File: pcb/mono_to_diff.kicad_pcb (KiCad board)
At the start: 4 copper layers, 88.9 x 88.9 mm, 48 parts, among them J1 24.243.1, J2 132134, J3 24.243.5, J4 132134, J5 24.243.2, J6 132134, J7 132134, U1 LT6656ACS6-1.25, U2 LTC6241HVCS8, U3 LT6600CS8-2.5

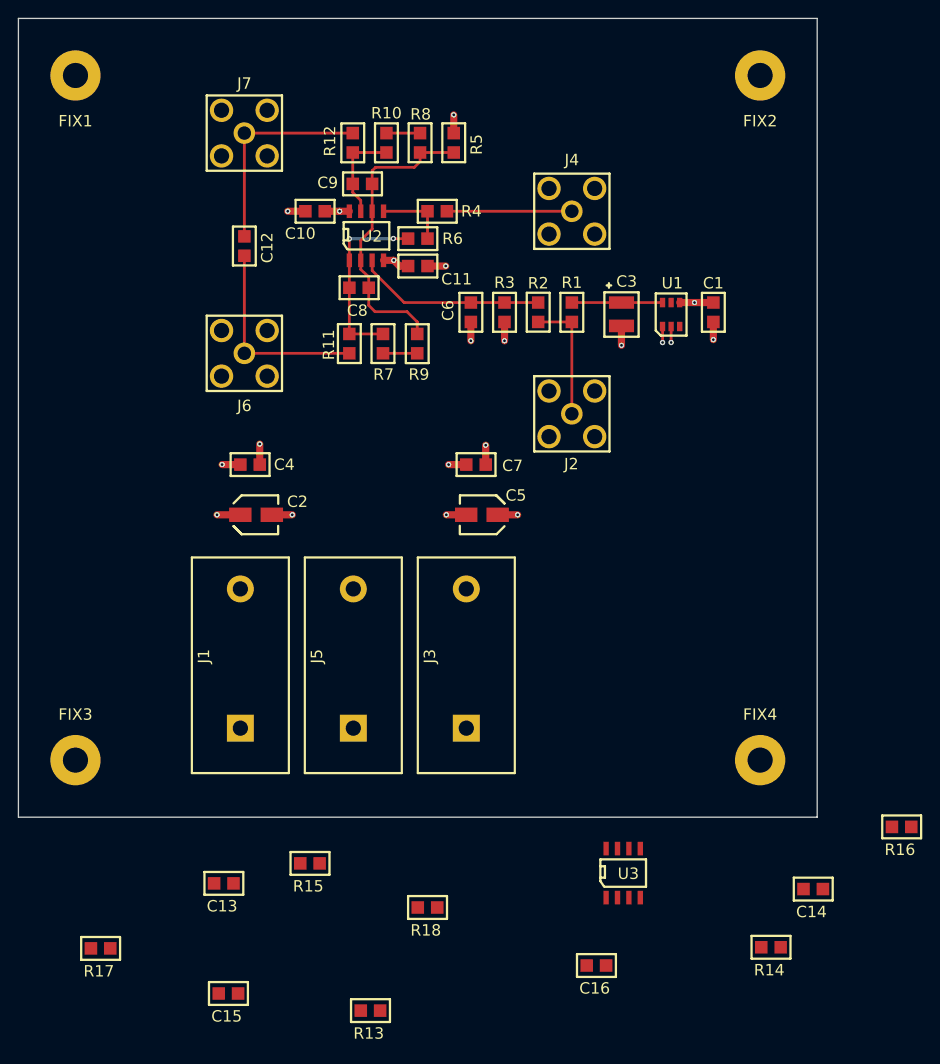
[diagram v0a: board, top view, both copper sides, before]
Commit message: PCB routed
 On branch development

	modified:   pcb/mono_to_diff.kicad_pcb
	modified:   pcb/mono_to_diff.pro
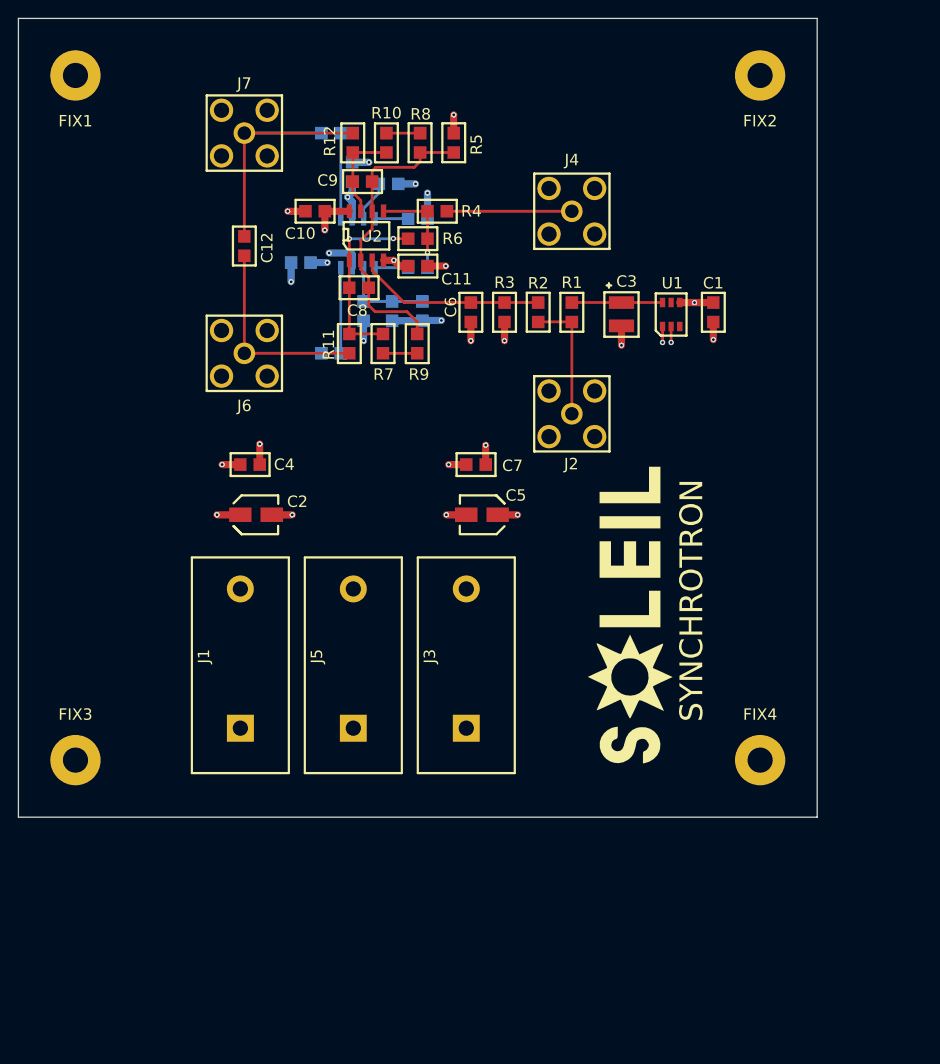
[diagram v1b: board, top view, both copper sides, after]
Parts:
- added G***: logo_soleil_400, logo:logo_soleil_400, F.Cu at (184.8, 119.7)
- C13, C14, C15, C16, R13, R14, R15, R16, R17, R18, U3: moved to B.Cu
- moved C14 91.6 mm to (157.0, 71.8)
- moved C16 91.1 mm to (154.0, 71.5), turned to 90 degrees
- moved R18 86.6 mm to (152.7, 66.1), turned to 180 degrees
- moved R16 85.2 mm to (162.4, 75.6), turned to 180 degrees
- moved R14 82.8 mm to (158.4, 84.8), turned to 270 degrees
- moved C15 82.0 mm to (149.4, 80.5), turned to 180 degrees
- moved R13 76.8 mm to (155.3, 87.0), turned to 90 degrees
- moved U3 74.7 mm to (156.5, 81.1), turned to 180 degrees
- moved R17 71.8 mm to (152.7, 90.6), turned to 180 degrees
- moved C13 68.8 mm to (161.8, 84.8), turned to 270 degrees
- moved R15 67.8 mm to (162.4, 81.1), turned to 180 degrees
- moved C9 0.25 mm to (154.1, 71.5)
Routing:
- net GND: track 26.9 -> 41.1 mm, vias 13 -> 18
- net VCC: track 11.1 -> 21.4 mm, vias 4 -> 7
- net Net-(C13-Pad1): track 0.00 -> 10.3 mm
- net Net-(R18-Pad1): track 0.00 -> 9.53 mm
- net Net-(R17-Pad1): track 0.00 -> 9.53 mm
- net /OUT_P: track 22.5 -> 31.1 mm
- net /OUT_N: track 23.6 -> 32.1 mm
- net Net-(C14-Pad1): track 0.00 -> 4.58 mm
- net VDD: track 7.18 -> 11.7 mm, vias 3 -> 4
- net Net-(R16-Pad2): track 0.00 -> 3.68 mm
- net Net-(R15-Pad2): track 0.00 -> 3.68 mm
- net Net-(R15-Pad1): track 7.94 -> 11.2 mm, vias 0 -> 1
- added copper zone on VCC-3.Cu, net VCC
- added copper zone on VCC-3.Cu, net VDD
- removed copper zone on VCC-4.Cu, net VCC
- removed copper zone on VCC-4.Cu, net VDD
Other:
- rule pad_to_mask_clearance: 0 -> 0.254
- board text added: "D = 2.8 mm"
- board text added: "SYNCHROTRON"

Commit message: Added a low pass filter
 On branch development

	modified:   pcb/mono_to_diff.kicad_pcb
	modified:   pcb/mono_to_diff.net
	modified:   sch/mono_to_diff-cache.lib
	modified:   sch/mono_to_diff.pro
	modified:   sch/mono_to_diff.sch
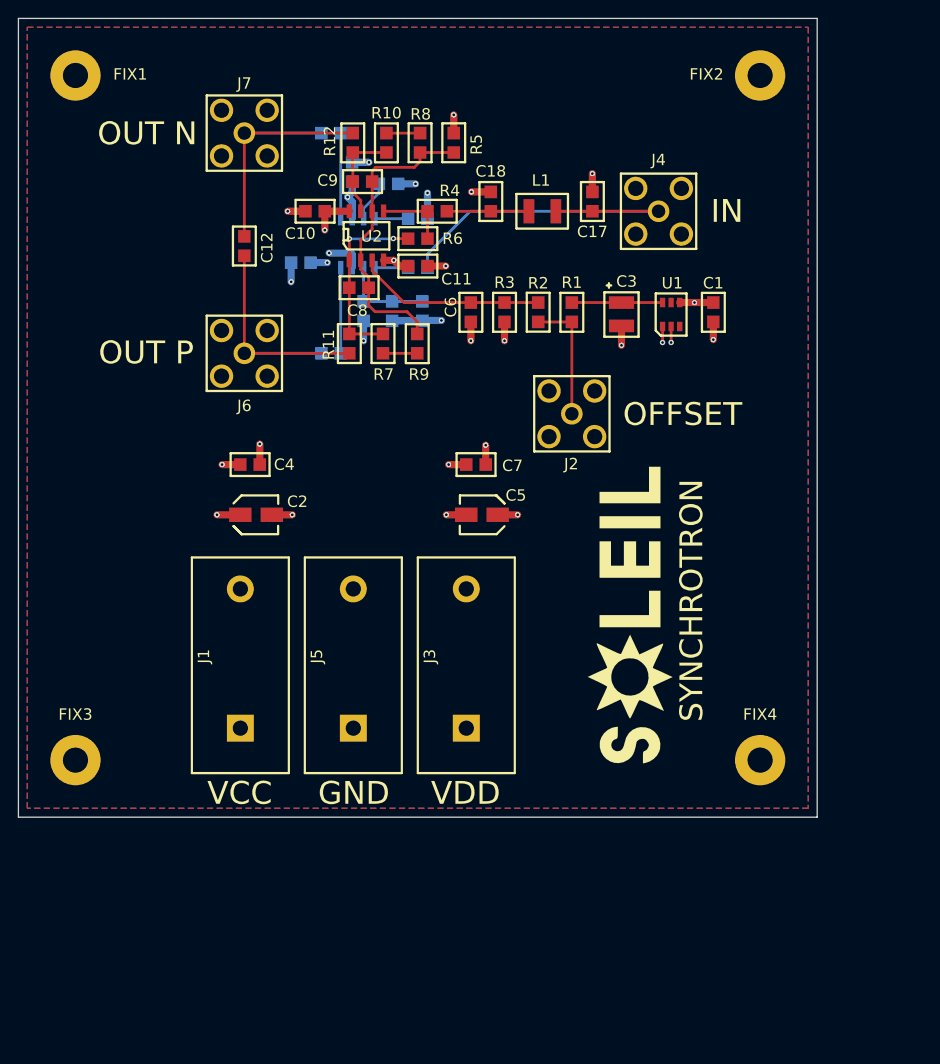
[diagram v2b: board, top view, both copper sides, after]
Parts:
- added C17: 2200pF-50V-5p-Ceramic-0805, RCL_SMT:SOLEIL-0805, F.Cu at (180.7, 74.8)
- added C18: 2200pF-50V-5p-Ceramic-0805, RCL_SMT:SOLEIL-0805, F.Cu at (169.4, 74.8)
- added L1: 10uH-140mA-5p-36MHz-1210, RCL_SMT:SOLEIL-1210, F.Cu at (176.7, 74.8)
- moved J4 9.65 mm to (188.1, 74.8)
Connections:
- J4 pad 1: Net-(J4-Pad1) -> Net-(C17-Pad1)
- R15 pad 1: Net-(R15-Pad1) -> Net-(C17-Pad1)
- R4 pad 1: Net-(R15-Pad1) -> Net-(R4-Pad1)
- R4 pad 2: Net-(J4-Pad1) -> Net-(C18-Pad1)
- R6 pad 2: Net-(R15-Pad1) -> Net-(R4-Pad1)
- U2 pad 5: Net-(R15-Pad1) -> Net-(R4-Pad1)
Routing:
- net Net-(C17-Pad1): track 0.00 -> 40.6 mm
- net Net-(J4-Pad1): track 13.9 -> 0.00 mm
- net Net-(R15-Pad1): track 11.2 -> 0.00 mm, vias 1 -> 0
- net Net-(C18-Pad1): track 0.00 -> 9.13 mm
- net Net-(R4-Pad1): track 0.00 -> 7.94 mm
- net GND: track 41.1 -> 45.3 mm, vias 18 -> 20
- added copper zone on B.Cu, net GND
- added copper zone on F.Cu, net GND
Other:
- board text added: "GND"
- board text added: "IN"
- board text added: "OFFSET"
- board text added: "OUT N"
- board text added: "OUT P"
- board text added: "VCC"
- board text added: "VDD"

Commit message: PCB finished
 On branch development

	modified:   README.md
	new file:   pcb/gerber/mono_to_diff-Bottom-4_Cu.gbl
	new file:   pcb/gerber/mono_to_diff-Bottom-4_Mask.gbs
	new file:   pcb/gerber/mono_to_diff-Bottom-4_Paste.gbp
	new file:   pcb/gerber/mono_to_diff-Bottom-4_SilkS.gbo
	new file:   pcb/gerber/mono_to_diff-Dwgs_User.gbr
	new file:   pcb/gerber/mono_to_diff-Edge_Cuts.gbr
	new file:   pcb/gerber/mono_to_diff-GND-2_Cu.gbr
	new file:   pcb/gerber/mono_to_diff-Margin.gbr
	new file:   pcb/gerber/mono_to_diff-Top-1_Cu.gtl
	new file:   pcb/gerber/mono_to_diff-Top-1_Mask.gts
	new file:   pcb/gerber/mono_to_diff-Top-1_Paste.gtp
	new file:   pcb/gerber/mono_to_diff-Top-1_SilkS.gto
	new file:   pcb/gerber/mono_to_diff-VCC-3_Cu.gbr
	new file:   pcb/gerber/mono_to_diff-bottom.pos
	new file:   pcb/gerber/mono_to_diff-drl.rpt
	new file:   pcb/gerber/mono_to_diff-drl_map.gbr
	new file:   pcb/gerber/mono_to_diff-top.pos
	new file:   pcb/gerber/mono_to_diff.drl
	modified:   pcb/mono_to_diff.kicad_pcb
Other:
- board text added: "1"
- board text added: "2"
- board text added: "3"
- board text added: "4"
- board text added: "Mono to Diff Convertor"
